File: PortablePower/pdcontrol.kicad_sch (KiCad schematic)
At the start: 19 parts, among them IC1 SW6208, J1 USB1130-15-A, J2 2137160001, Q1 CSD17313Q2, Q2 CSD17313Q2, U1 USBLC6-2SC6, U2 USBLC6-2SC6

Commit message: almost done with pd control
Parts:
- added C11: 22uf/10v, Capacitor_SMD:C_0603_1608Metric_Pad1.08x0.95mm_HandSolder, symbol Device:C
- added D1, D2, D3, D4, D5, D6: LED, LED_SMD:LED_1206_3216Metric_Pad1.42x1.75mm_HandSolder, symbol Device:LED
- added R2, R3: 10k, Resistor_SMD:R_0603_1608Metric_Pad0.98x0.95mm_HandSolder, symbol Device:R
- added R4: 330, Resistor_SMD:R_0805_2012Metric_Pad1.20x1.40mm_HandSolder, symbol Device:R
- added R5: 26.7k, Resistor_SMD:R_0603_1608Metric_Pad0.98x0.95mm_HandSolder, symbol Device:R
- added S1: B3U1000P, B3U1000P:B3U-1000P, symbol B3U1000P:B3U1000P
- added TP1: NTC, Connector_PinHeader_2.00mm:PinHeader_2x01_P2.00mm_Vertical, symbol Connector:TestPoint_2Pole
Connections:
- net +VDC is gone; now on net +BATT: C1.1, C2.1, L1.1
- net VOUTP is gone; now on net VOUTA1: C6.1, C7.2, IC1.27 (VOUTSP), Q1.1 (D), Q1.2 (D), Q1.5 (D), Q1.6 (D), Q1.8 (D), Q2.1 (D), Q2.2 (D), Q2.5 (D), Q2.6 (D), Q2.8 (D), R1.1
- net BST: now also IC1.7 (BST)
- net GND: now also IC1.49 (EP), C11.2, R5.2, S1.2 (NO), TP1.1
- net SW: now also IC1.2 (SW_1), IC1.3 (SW_2), IC1.4 (SW_3), IC1.5 (SW_4), IC1.6 (SW_5)
- net DC-: now reaches U1.4 (I/O2)
- net DC-: now also IC1.42 (DMC)
- net DC+: now reaches U1.6 (I/O1)
- net DC+: now also IC1.43 (DPC)
- net VBUSA1: now reaches IC1.10 (VBUSA1)
- net VBUSA1: now also C5.1, J1.1 (VCC), Q2.4 (S), Q2.7 (S)
- net VBUSC: now reaches IC1.12 (VBUSC)
- net VBUSC: now also C4.1, J2.A4 (VBUS1), J2.A9 (VBUS2), J2.B4 (VBUS3), J2.B9 (VBUS4), Q1.4 (S), Q1.7 (S)
- net VOUTA1: now reaches IC1.13 (VOUTC)
- net VOUTA1: now also IC1.9 (VOUTA1)
- net +BATT: now reaches IC1.17 (BAT)
- net at IC1.18 (NTC): now also TP1.2
- net VCC: now reaches IC1.19 (VCC)
- net VCC: now also C11.1, R2.2, R3.2, R4.2
- net at IC1.20 (KEY/GSET/IDA1): now also R2.1, S1.1 (COM)
- net at IC1.21 (FLED/BSET/IDA2): now also D1.1 (K), R3.1
- net at IC1.22 (LED5/CSET): now also R5.1
- net at IC1.23 (LED4/I2C): now also D6.2 (A)
- net at IC1.24 (LED3/IRQ): now also D4.1 (K), D5.2 (A)
- net at IC1.25 (LED2/SDA): now also D2.1 (K), D3.2 (A)
- net DLED1: now reaches IC1.26 (LED1/SCK)
- net DLED1: now also D2.2 (A), D3.1 (K), D4.2 (A), D5.1 (K), D6.1 (K)
- net CC2: now reaches IC1.40 (CC2)
- net CC2: now also J2.B5 (CC2)
- net CC1: now reaches IC1.41 (CC1)
- net CC1: now also J2.A5 (CC1)
- net DA-: now reaches IC1.46 (DMA1)
- net DA-: now also U2.6 (I/O1)
- net DA+: now reaches IC1.47 (DPA1)
- net DA+: now also U2.4 (I/O2)
- new net: D1.2 (A), R4.1
- no-connect marks 0 -> 3
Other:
- note added: "RBSET 4.2V"
- note added: "RCSET 26.583=26.7 equivalent"

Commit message: schematic complete
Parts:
- added TP10: DATA, TestPoint:TestPoint_Pad_D1.0mm, symbol Connector:TestPoint
- added TP11: CCL/WLED, TestPoint:TestPoint_Pad_D1.0mm, symbol Connector:TestPoint
- added TP2: VBUSL, TestPoint:TestPoint_Pad_D1.0mm, symbol Connector:TestPoint
- added TP3: VBUSS2, TestPoint:TestPoint_Pad_D1.0mm, symbol Connector:TestPoint
- added TP4: VOUTA2, TestPoint:TestPoint_Pad_D1.0mm, symbol Connector:TestPoint
- added TP5: DMA2, TestPoint:TestPoint_Pad_D1.0mm, symbol Connector:TestPoint
- added TP6: DPA2, TestPoint:TestPoint_Pad_D1.0mm, symbol Connector:TestPoint
- added TP7: DPB, TestPoint:TestPoint_Pad_D1.0mm, symbol Connector:TestPoint
- added TP8: DMB, TestPoint:TestPoint_Pad_D1.0mm, symbol Connector:TestPoint
- added TP9: VBUSB, TestPoint:TestPoint_Pad_D1.0mm, symbol Connector:TestPoint
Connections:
- net at IC1.1 (DPA2): now also TP6.1
- net at IC1.11 (VBUSB): now also TP9.1
- net at IC1.14 (VOUTA2): now also TP4.1
- net at IC1.15 (VBUSA2): now also TP3.1
- net at IC1.16 (VBUSL): now also TP2.1
- net at IC1.39 (CCL/WLED): now also TP11.1
- net at IC1.44 (DMB): now also TP8.1
- net at IC1.45 (DPB): now also TP7.1
- net at IC1.48 (DMA2): now also TP5.1
- net at IC1.8 (DATA): now also TP10.1
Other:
- note added: "RBset=( Cset + 2000 )*5/3 Cset = mah RBset = Ohm"
- note added: "When FLED/BSET/IDA2 is pulledup to VCCwith a 10KΩ resister, 4.2V is set; When selecting a 15KΩ resister, 4.35V is set; When selecting a 5.6KΩ resister, 4.4V is set; When selecting a 3KΩ resister, 4.5V is set"
- moved on the sheet: C10, C11, C4, C5, C6, C7, C8, C9, D1, D2, D3, D4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

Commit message: randome one
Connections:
- net VBUSA1: now also U2.5 (VBUS)
- net VBUSC: now also U1.5 (VBUS)
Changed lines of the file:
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@@
+	(wire
+		(pts
+			(xy 93.98 144.145) (xy 93.98 151.765)
+		)
+		(stroke
+			(width 0)
+			(type default)
+		)
+	)
 	(wire
 		(pts
@@
 		(pts
 			(xy 78.105 184.785) (xy 80.645 184.785)
+		)
+		(stroke
+			(width 0)
+			(type default)
+		)
+	)
+	(wire
+		(pts
+			(xy 76.2 60.325) (xy 76.2 68.58)
 		)
 		(stroke
@@
 		)
 	)
+	(label "VBUSC"
+		(at 93.98 144.145 270)
+		(effects
+			(font
+				(size 1.27 1.27)
+			)
+			(justify right bottom)
+		)
+	)
 	(label "D-"
 		(at 67.945 73.66 0)
@@
 		)
 	)
+	(label "VBUSA1"
+		(at 76.2 60.325 270)
+		(effects
+			(font
+				(size 1.27 1.27)
+			)
+			(justify right bottom)
+		)
+	)

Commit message: halfway through pd everything
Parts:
- removed TP7: DPB, TestPoint:TestPoint_Pad_D1.0mm, symbol Connector:TestPoint
- removed TP8: DMB, TestPoint:TestPoint_Pad_D1.0mm, symbol Connector:TestPoint
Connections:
- net D+: now also U2.1 (I/O1); no longer U2.3 (I/O2)
- net D-: now also U2.3 (I/O2); no longer U2.1 (I/O1)
- net D1+: now also U1.3 (I/O2); no longer U1.1 (I/O1)
- net D1-: now also U1.1 (I/O1); no longer U1.3 (I/O2)
- net DA+: now also U2.6 (I/O1); no longer U2.4 (I/O2)
- net DA-: now also U2.4 (I/O2); no longer U2.6 (I/O1)
- net DC+: now also U1.4 (I/O2); no longer U1.6 (I/O1)
- net DC-: now also U1.6 (I/O1); no longer U1.4 (I/O2)
- no-connect marks 3 -> 5

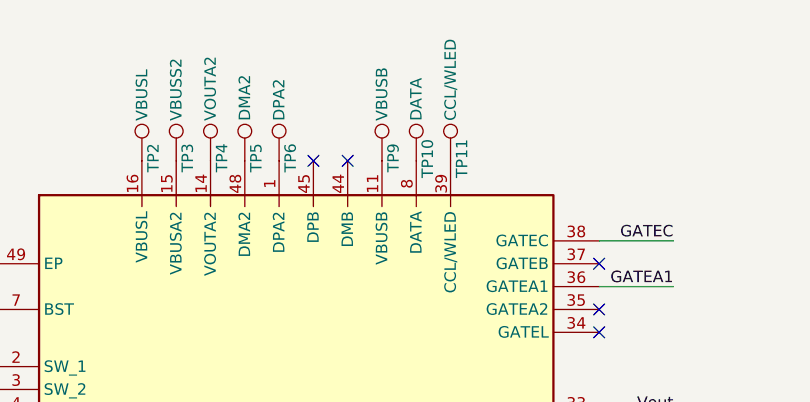
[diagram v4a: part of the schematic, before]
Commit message: mostly done on pd layout
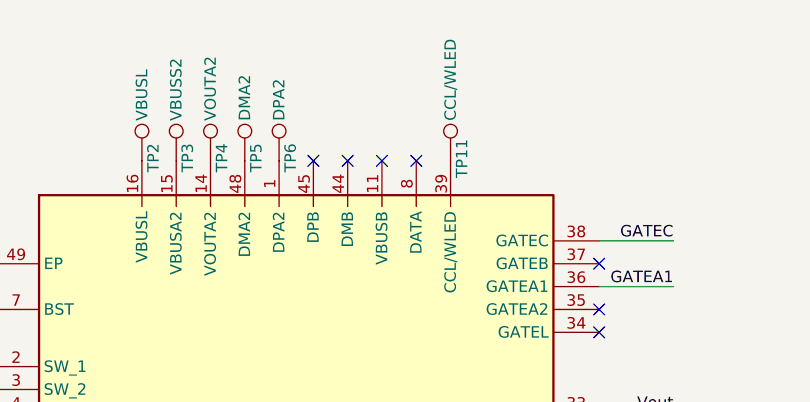
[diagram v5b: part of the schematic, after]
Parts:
- removed TP10: DATA, TestPoint:TestPoint_Pad_D1.0mm, symbol Connector:TestPoint
- removed TP9: VBUSB, TestPoint:TestPoint_Pad_D1.0mm, symbol Connector:TestPoint
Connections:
- no-connect marks 5 -> 7
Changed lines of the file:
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@@
 	)
 	(no_connect
+		(at 168.275 35.56)
+	)
+	(no_connect
 		(at 188.595 46.99)
 	)
 	(no_connect
+		(at 164.465 35.56)
+	)
+	(no_connect
 		(at 160.655 35.56)
 	)
@@
 	)
 	(symbol
-		(lib_id "Connector:TestPoint")
-		(at 168.275 35.56 0)
-		(unit 1)
-		(exclude_from_sim no)
-		(in_bom yes)
-		(on_board yes)
-		(dnp no)
-		(property "Reference" "TP10"
-			(at 169.545 37.465 90)
-			(effects
-				(font
-					(size 1.27 1.27)
-				)
-				(justify left)
-			)
-		)
-		(property "Value" "DATA"
-			(at 168.275 31.115 90)
-			(effects
-				(font
-					(size 1.27 1.27)
-				)
-				(justify left)
-			)
-		)
-		(property "Footprint" "TestPoint:TestPoint_Pad_D1.0mm"
-			(at 173.355 35.56 0)
-			(effects
-				(font
-					(size 1.27 1.27)
-				)
-				(hide yes)
-			)
-		)
-		(property "Datasheet" "~"
-			(at 173.355 35.56 0)
-			(effects
-				(font
-					(size 1.27 1.27)
-				)
-				(hide yes)
-			)
-		)
-		(property "Description" "test point"
-			(at 168.275 35.56 0)
-			(effects
-				(font
-					(size 1.27 1.27)
-				)
-				(hide yes)
-			)
-		)
-		(pin "1"
-		)
-		(instances
-			(project "PortablePower"
-				(path "/4474177b-2e5c-4472-8e6c-d549a0d6c1d6/6fa13e06-34db-49b7-a023-450a8ba3031e"
-					(reference "TP10")
-					(unit 1)
-				)
-			)
-		)
-	)
-	(symbol
 		(lib_id "Device:C")
 		(at 145.415 180.975 0)
@@
 					(unit 1)
 				)
-			)
-		)
-	)
-	(symbol
-		(lib_id "Connector:TestPoint")
-		(at 164.465 35.56 0)
-		(unit 1)
-		(exclude_from_sim no)
-		(in_bom yes)
-		(on_board yes)
-		(dnp no)
-		(property "Reference" "TP9"
-			(at 165.735 36.83 90)
-			(effects
-				(font
-					(size 1.27 1.27)
-				)
-				(justify left)
-			)
-		)
-		(property "Value" "VBUSB"
-			(at 164.465 31.115 90)
-			(effects
-				(font
-					(size 1.27 1.27)
-				)
-				(justify left)
-			)
-		)
-		(property "Footprint" "TestPoint:TestPoint_Pad_D1.0mm"
-			(at 169.545 35.56 0)
-			(effects
-				(font
-					(size 1.27 1.27)
-				)
-				(hide yes)
-			)
-		)
-		(property "Datasheet" "~"
-			(at 169.545 35.56 0)
-			(effects
-				(font
-					(size 1.27 1.27)
-				)
-				(hide yes)
-			)
-		)
-		(property "Description" "test point"
-			(at 164.465 35.56 0)
-			(effects
-				(font
-					(size 1.27 1.27)
-				)
-				(hide yes)
-			)
-		)
-		(pin "1"
-		)
-		(instances
-			(project "PortablePower"
-				(path "/4474177b-2e5c-4472-8e6c-d549a0d6c1d6/6fa13e06-34db-49b7-a023-450a8ba3031e"
-					(reference "TP9")
-					(unit 1)
-				)

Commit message: pc done
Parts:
- removed TP11: CCL/WLED, TestPoint:TestPoint_Pad_D1.0mm, symbol Connector:TestPoint
- removed TP2: VBUSL, TestPoint:TestPoint_Pad_D1.0mm, symbol Connector:TestPoint
- removed TP3: VBUSS2, TestPoint:TestPoint_Pad_D1.0mm, symbol Connector:TestPoint
- removed TP4: VOUTA2, TestPoint:TestPoint_Pad_D1.0mm, symbol Connector:TestPoint
- removed TP5: DMA2, TestPoint:TestPoint_Pad_D1.0mm, symbol Connector:TestPoint
- removed TP6: DPA2, TestPoint:TestPoint_Pad_D1.0mm, symbol Connector:TestPoint
- added H1: MountingHole, MountingHole:MountingHole_2.2mm_M2, symbol Mechanical:MountingHole
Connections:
- net DLED1: now also D2.1 (K), D3.2 (A), D4.1 (K), D5.2 (A); no longer D2.2 (A), D3.1 (K), D4.2 (A), D5.1 (K)
- new net: D2.2 (A), D3.1 (K), IC1.25 (LED2/SDA)
- new net: D4.2 (A), D5.1 (K), IC1.24 (LED3/IRQ)
- no-connect marks 7 -> 13
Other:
- company: (none) -> Mekatra
- title: (none) -> PowerBank
- moved on the sheet: D2, D3, D4, D5

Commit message: added logo
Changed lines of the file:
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@@
+	)
+	(symbol
+		(lib_id "Mekatra symbol kicad:LOGO")
+		(at 256.54 154.94 0)
+		(unit 1)
+		(exclude_from_sim no)
+		(in_bom yes)
+		(on_board yes)
+		(dnp no)
+		(fields_autoplaced yes)
+		(property "Reference" "#G1"
+			(at 256.54 147.9876 0)
+			(effects
+				(font
+					(size 1.27 1.27)
+				)
+				(hide yes)
+			)
+		)
+		(property "Value" "LOGO"
+			(at 256.54 161.8924 0)
+			(effects
+				(font
+					(size 1.27 1.27)
+				)
+				(hide yes)
+			)
+		)
+		(property "Footprint" ""
+			(at 256.54 154.94 0)
+			(effects
+				(font
+					(size 1.27 1.27)
+				)
+				(hide yes)
+			)
+		)
+		(property "Datasheet" ""
+			(at 256.54 154.94 0)
+			(effects
+				(font
+					(size 1.27 1.27)
+				)
+				(hide yes)
+			)
+		)
+		(property "Description" ""
+			(at 256.54 154.94 0)
+			(effects
+				(font
+					(size 1.27 1.27)
+				)
+				(hide yes)
+			)
+		)
+		(instances
+			(project ""
+				(path "/4474177b-2e5c-4472-8e6c-d549a0d6c1d6/6fa13e06-34db-49b7-a023-450a8ba3031e"
+					(reference "#G1")
+					(unit 1)
+				)
+			)
+		)
 	)
 	(symbol
